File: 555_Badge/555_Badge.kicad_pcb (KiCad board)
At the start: 2 copper layers, 15 parts, among them Q1 2N3904, U1 7555

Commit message: setup pcb layout
added jclpcb drc design rule
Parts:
- moved S1 3.61 mm to (117.0, 93.4)
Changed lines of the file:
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@@
   )
   (paper "A4")
+  (title_block
+    (title "555 Badge")
+    (rev "V1")
+    (comment 2 "License: CC by 4.0")
+    (comment 3 "Author: Glenn Lopez")
+  )
   (layers
     (0 "F.Cu" signal)
@@
   )
   (footprint "digikey-footprints:Switch_Slide_11.6x4mm_EG1218" (layer "F.Cu")
-    (at 120.6076 93.43)
+    (at 117 93.4)
     (descr "http://spec_sheets.e-switch.com/specs/P040040.pdf")
     (property "Category" "Switches")

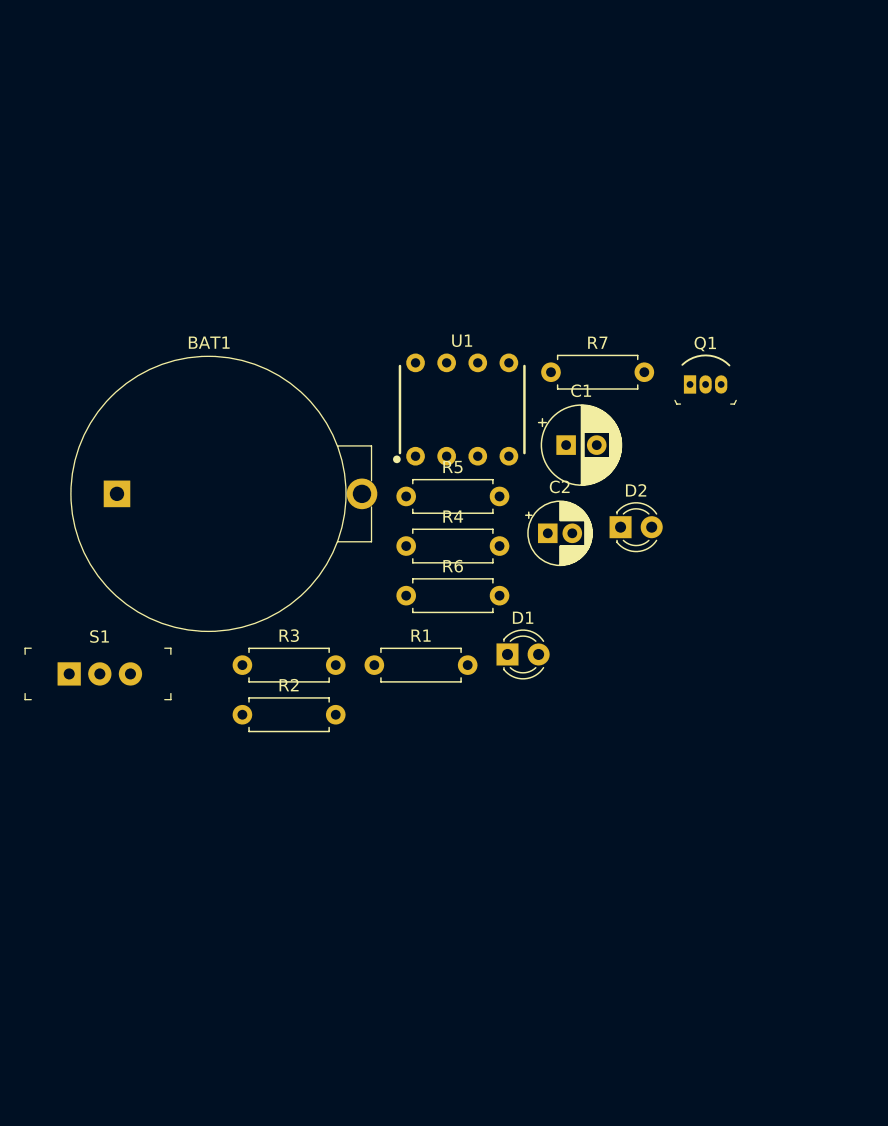
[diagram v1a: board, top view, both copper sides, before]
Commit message: pcb parts placement and board outline definition
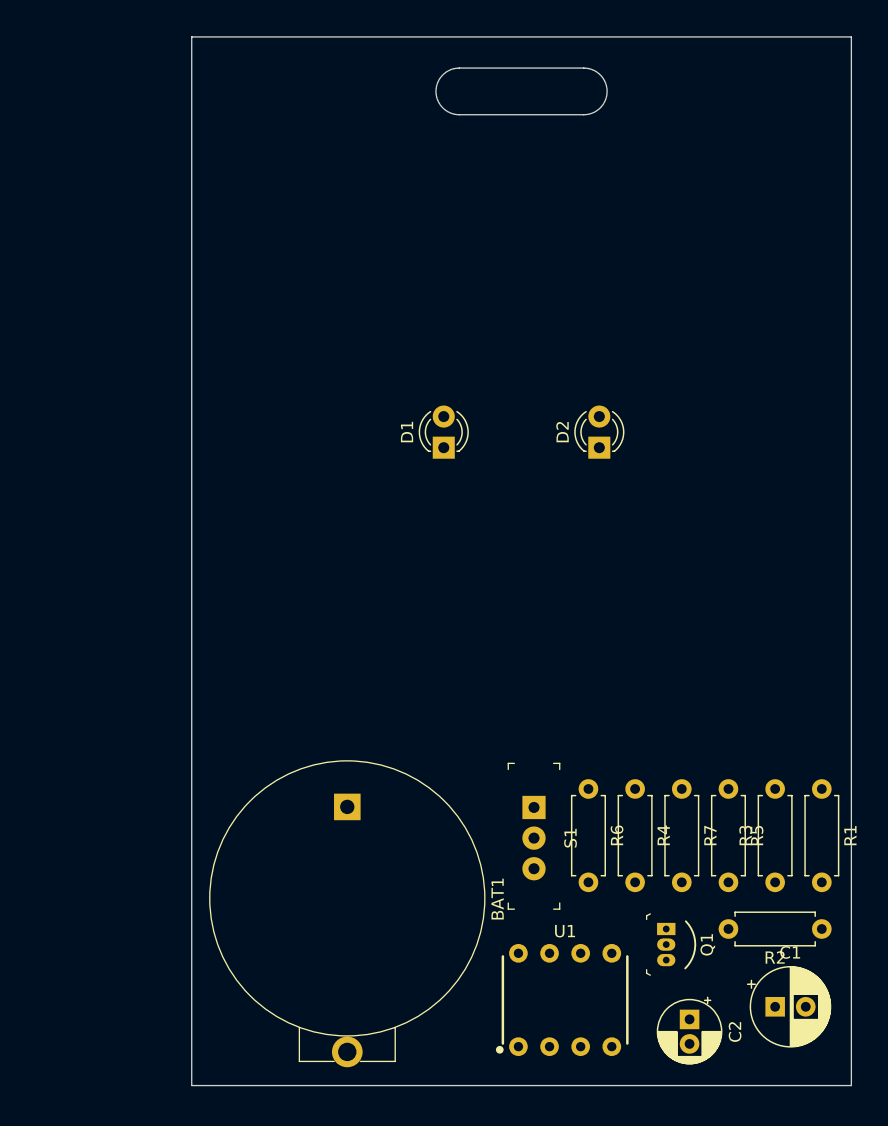
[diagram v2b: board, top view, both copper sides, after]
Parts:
- moved R2 50.4 mm to (178.4, 114.2), turned to 180 degrees
- moved U1 48.9 mm to (157.5, 120.0)
- moved C1 48.9 mm to (174.6, 120.6)
- moved R3 47.0 mm to (174.6, 110.4), turned to 90 degrees
- moved Q1 44.5 mm to (165.7, 114.2), turned to -90 degrees
- moved C2 41.3 mm to (167.6, 121.6), turned to -90 degrees
- moved S1 39.5 mm to (154.9, 104.3), turned to -90 degrees
- moved R1 37.9 mm to (178.4, 102.8), turned to -90 degrees
- moved R7 35.7 mm to (167.0, 102.8), turned to -90 degrees
- moved R5 35.5 mm to (170.8, 102.8), turned to -90 degrees
- moved BAT1 31.7 mm to (139.7, 104.3), turned to -90 degrees
- moved R4 27.2 mm to (163.2, 102.8), turned to -90 degrees
- moved R6 21.7 mm to (159.4, 102.8), turned to -90 degrees
- moved D1 17.7 mm to (147.6, 74.9), turned to 90 degrees
- moved D2 6.72 mm to (160.3, 74.9), turned to 90 degrees
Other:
- board outline added: 53.8 x 85.6 mm

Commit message: boardlayout complete
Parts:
- moved BAT1 17.6 mm to (139.2, 121.8), turned to 90 degrees
- moved R2 13.6 mm to (170.9, 102.9), turned to -90 degrees
- moved R5 12.8 mm to (171.2, 115.6), turned to 0 degrees
- moved S1 5.07 mm to (154.2, 109.3), turned to 90 degrees
- moved C1 1.22 mm to (175.8, 121.0), turned to -90 degrees
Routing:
- net Net-(D1-Pad2): track 0.00 -> 60.1 mm
- net Net-(D1-Pad1): track 0.00 -> 56.9 mm
- net VCC: track 0.00 -> 48.0 mm
- net Net-(D2-Pad2): track 0.00 -> 34.9 mm
- net Net-(R3-Pad2): track 0.00 -> 31.5 mm
- net Net-(U1-Pad2): track 0.00 -> 31.1 mm
- net Net-(C1-Pad1): track 0.00 -> 24.4 mm
- net Net-(R4-Pad1): track 0.00 -> 22.9 mm
- net Net-(BAT1-PadPos): track 0.00 -> 16.0 mm
- net Net-(Q1-Pad2): track 0.00 -> 5.49 mm
- added copper zone on B.Cu, net GND
- added copper zone on F.Cu, net GND
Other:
- board text added: "555 Badge"
- board text added: "v1"
